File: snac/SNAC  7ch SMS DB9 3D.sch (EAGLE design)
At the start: 43 parts, among them IC1 4030D, K2 692112030100, Q1 BSS138, Q2 BSS138, Q3 BSS138, Q4 BSS138, Q5 BSS138, Q6 BSS138, Q7 BSS138, Q8 BSS138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

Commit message: Added combined voltage translation + SNES joyport
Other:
- note removed: "USB Controller"
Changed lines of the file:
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@@
 <wire x1="127" y1="172.72" x2="0" y2="172.72" width="0.2032" layer="95" style="longdash"/>
 <wire x1="248.92" y1="172.72" x2="127" y2="172.72" width="0.2032" layer="95" style="longdash"/>
-<text x="98.806" y="113.03" size="3.302" layer="95">USB Controller</text>
 <text x="164.846" y="113.03" size="3.302" layer="95">USB Mister</text>
 <text x="17.526" y="41.91" size="1.778" layer="95">size 0805</text>
@@
 </segment>
 <segment>
-<wire x1="124.46" y1="86.36" x2="129.54" y2="86.36" width="0.1524" layer="91"/>
-<label x="129.54" y="86.36" size="1.27" layer="95" xref="yes"/>
-</segment>
-<segment>
 <pinref part="X3" gate="-6" pin="F"/>
 <wire x1="358.14" y1="162.56" x2="347.98" y2="162.56" width="0.1524" layer="91"/>
@@
 </segment>
 <segment>
-<wire x1="124.46" y1="101.6" x2="129.54" y2="101.6" width="0.1524" layer="91"/>
-<label x="129.54" y="101.6" size="1.27" layer="95" xref="yes"/>
-</segment>
-<segment>
 <pinref part="X3" gate="-1" pin="F"/>
 <wire x1="358.14" y1="175.26" x2="347.98" y2="175.26" width="0.1524" layer="91"/>
@@
 <wire x1="53.34" y1="91.44" x2="60.96" y2="91.44" width="0.1524" layer="91"/>
 <label x="60.96" y="91.44" size="1.27" layer="95" xref="yes"/>
-</segment>
-<segment>
-<wire x1="124.46" y1="104.14" x2="129.54" y2="104.14" width="0.1524" layer="91"/>
-<label x="129.54" y="104.14" size="1.27" layer="95" xref="yes"/>
 </segment>
 <segment>
@@
 </segment>
 <segment>
-<wire x1="124.46" y1="88.9" x2="129.54" y2="88.9" width="0.1524" layer="91"/>
-<label x="129.54" y="88.9" size="1.27" layer="95" xref="yes"/>
-</segment>
-<segment>
 <pinref part="X3" gate="-4" pin="F"/>
 <wire x1="358.14" y1="167.64" x2="347.98" y2="167.64" width="0.1524" layer="91"/>
@@
 </segment>
 <segment>
-<wire x1="124.46" y1="99.06" x2="129.54" y2="99.06" width="0.1524" layer="91"/>
-<label x="129.54" y="99.06" size="1.27" layer="95" xref="yes"/>
-</segment>
-<segment>
 <pinref part="X3" gate="-2" pin="F"/>
 <wire x1="358.14" y1="172.72" x2="347.98" y2="172.72" width="0.1524" layer="91"/>
@@
 </segment>
 <segment>
-<wire x1="124.46" y1="91.44" x2="129.54" y2="91.44" width="0.1524" layer="91"/>
-<label x="129.54" y="91.44" size="1.27" layer="95" xref="yes"/>
-</segment>
-<segment>
 <pinref part="X3" gate="-7" pin="F"/>
 <wire x1="358.14" y1="160.02" x2="347.98" y2="160.02" width="0.1524" layer="91"/>
@@
 </segment>
 <segment>
-<wire x1="124.46" y1="93.98" x2="129.54" y2="93.98" width="0.1524" layer="91"/>
-<label x="129.54" y="93.98" size="1.27" layer="95" xref="yes"/>
-</segment>
-<segment>
 <pinref part="X3" gate="-3" pin="F"/>
 <wire x1="358.14" y1="170.18" x2="347.98" y2="170.18" width="0.1524" layer="91"/>
@@
 </segment>
 <segment>
-<wire x1="124.46" y1="83.82" x2="129.54" y2="83.82" width="0.1524" layer="91"/>
-<label x="129.54" y="83.82" size="1.27" layer="95" xref="yes"/>
-</segment>
-<segment>
 <pinref part="X3" gate="-9" pin="F"/>
 <wire x1="358.14" y1="154.94" x2="347.98" y2="154.94" width="0.1524" layer="91"/>
@@
 </segment>
 <segment>
-<wire x1="124.46" y1="96.52" x2="129.54" y2="96.52" width="0.1524" layer="91"/>
-<label x="129.54" y="96.52" size="1.27" layer="95" xref="yes"/>
-</segment>
-<segment>

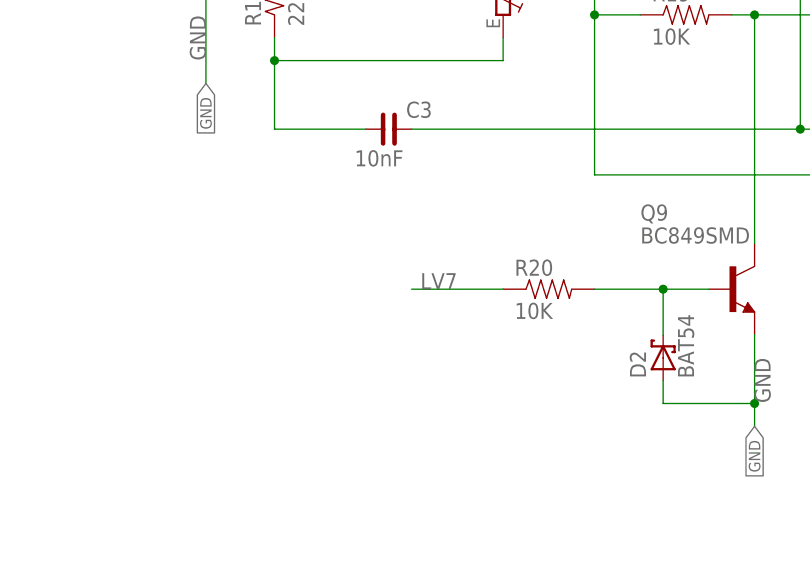
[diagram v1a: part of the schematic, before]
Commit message: changed from LV7 to LV5 pin, for the 3D Glasses boards
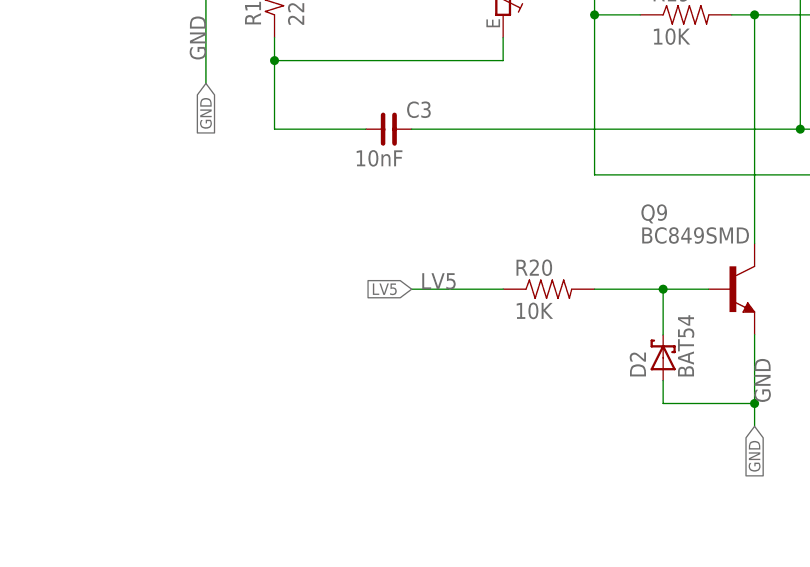
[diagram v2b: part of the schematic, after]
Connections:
- net LV5: now also R20.1
- net LV7: no longer R20.1
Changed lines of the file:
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@@
 <wire x1="187.96" y1="91.44" x2="193.04" y2="91.44" width="0.1524" layer="91"/>
 <label x="193.04" y="91.44" size="1.27" layer="95" xref="yes"/>
+<label x="325.12" y="73.66" size="1.27" layer="95" rot="MR0" xref="yes"/>
+</segment>
+<segment>
+<pinref part="R20" gate="G$1" pin="1"/>
+<wire x1="335.28" y1="73.66" x2="325.12" y2="73.66" width="0.1524" layer="91"/>
+<label x="330.2" y="73.66" size="1.778" layer="95" rot="MR0"/>
 </segment>
 </net>
@@
 <label x="116.84" y="55.88" size="1.27" layer="95" xref="yes"/>
 </segment>
-<segment>
-<pinref part="R20" gate="G$1" pin="1"/>
-<wire x1="335.28" y1="73.66" x2="325.12" y2="73.66" width="0.1524" layer="91"/>
-<label x="330.2" y="73.66" size="1.778" layer="95" rot="MR0"/>
-</segment>
 </net>
